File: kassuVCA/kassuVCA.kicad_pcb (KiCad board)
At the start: 2 copper layers, 49 x 59 mm, 20 parts, among them J1 Conn_02x05_Odd_Even, Q1 2N3904, Q2 2N3904, Q3 2N3904, U1 TL072

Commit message: switch to mbt3904 double transistor 2n3904 dual package
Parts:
- removed Q3: 2N3904, Package_TO_SOT_THT:TO-92L_Inline_Wide
- Q2: value 2N3904 -> MBT3904DW1; footprint Package_TO_SOT_THT:TO-92L_Inline_Wide -> Package_TO_SOT_SMD:SOT-363_SC-70-6
- moved Q2 2.51 mm to (125.5, 103.0), turned to 0 degrees
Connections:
- R10 pad 2: Net-(Q3-Pad3) -> Net-(Q2-Pad3)
- R11 pad 2: Net-(Q2-Pad3) -> Net-(Q2-Pad6)
- R12 pad 2: Net-(Q3-Pad3) -> Net-(Q2-Pad3)
- R7 pad 2: Net-(Q2-Pad3) -> Net-(Q2-Pad6)
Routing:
- net Net-(Q3-Pad3): track 60.0 -> 0.00 mm
- net Net-(Q2-Pad6): track 0.00 -> 37.9 mm
- net GND: track 0.00 -> 18.5 mm, vias 0 -> 1
- net Net-(Q2-Pad3): track 36.0 -> 50.3 mm
- net Net-(Q1-Pad1): track 47.5 -> 51.8 mm
- net Net-(R14-Pad1): track 35.7 -> 39.5 mm

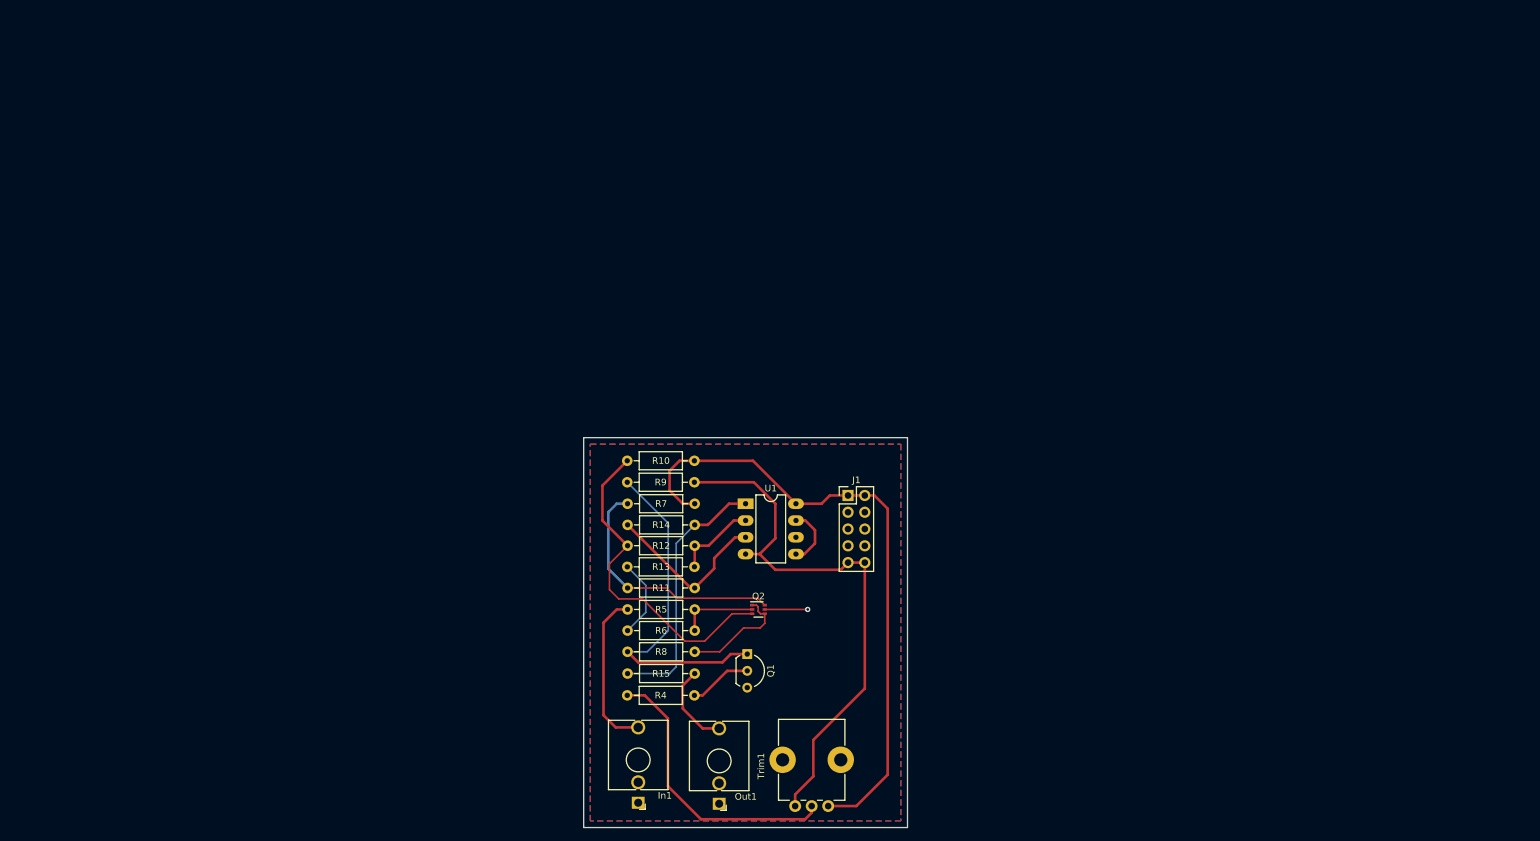
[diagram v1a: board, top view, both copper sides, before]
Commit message: VCA state working with jelly bean 2n3904 transistors
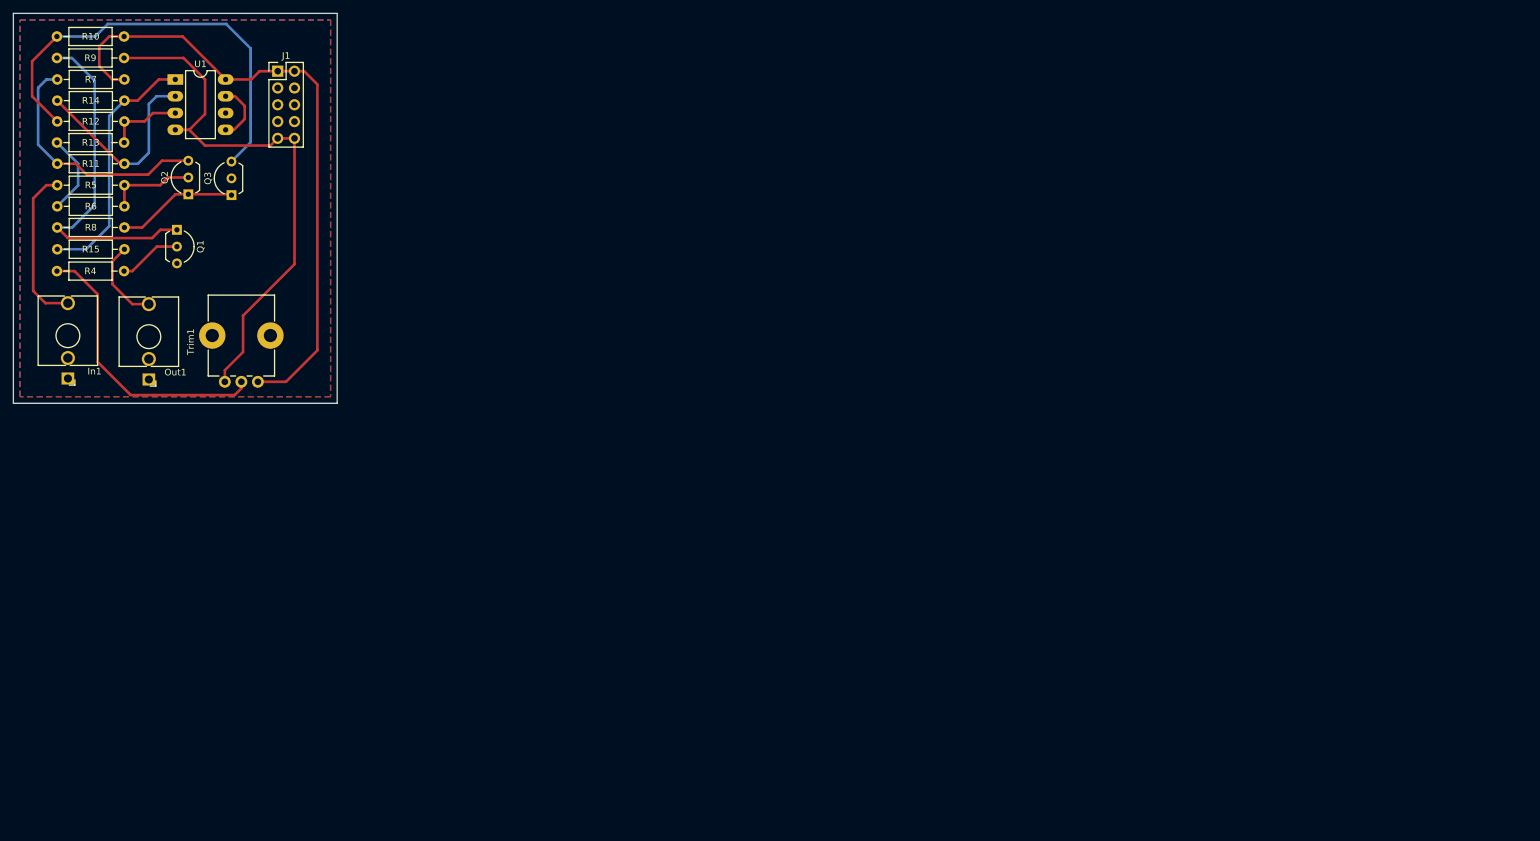
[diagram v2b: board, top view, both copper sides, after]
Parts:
- added Q3: 2N3904, Package_TO_SOT_THT:TO-92L_Inline_Wide, F.Cu at (45.7, 40.3)
- Q2: value MBT3904DW1 -> 2N3904; footprint Package_TO_SOT_SMD:SOT-363_SC-70-6 -> Package_TO_SOT_THT:TO-92L_Inline_Wide
- moved In1 107.6 mm to (20.9, 68.0)
- moved J1 107.6 mm to (52.7, 21.6)
- moved Out1 107.6 mm to (33.2, 68.2)
- moved Q1 107.6 mm to (37.5, 45.5)
- moved R10 107.6 mm to (29.4, 16.3)
- moved R11 107.6 mm to (29.5, 35.5)
- moved R12 107.6 mm to (29.5, 29.1)
- moved R13 107.6 mm to (19.3, 32.4)
- moved R14 107.6 mm to (29.5, 26.0)
- moved R15 107.6 mm to (19.3, 48.5)
- moved R4 107.6 mm to (29.4, 51.8)
- moved R5 107.6 mm to (29.5, 38.8)
- moved R6 107.6 mm to (19.3, 42.0)
- moved R7 107.6 mm to (29.5, 22.8)
- moved R8 107.6 mm to (29.5, 45.2)
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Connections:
- R10 pad 2: Net-(Q2-Pad3) -> Net-(Q3-Pad3)
- R11 pad 2: Net-(Q2-Pad6) -> Net-(Q2-Pad3)
- R12 pad 2: Net-(Q2-Pad3) -> Net-(Q3-Pad3)
- R7 pad 2: Net-(Q2-Pad6) -> Net-(Q2-Pad3)
- U1 pad 2: Net-(R12-Pad1) -> Net-(R11-Pad1)
- U1 pad 3: Net-(R11-Pad1) -> Net-(R12-Pad1)
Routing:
- net Net-(Q3-Pad3): track 0.00 -> 65.9 mm
- net Net-(Q2-Pad6): track 37.9 -> 0.00 mm
- net Net-(Q2-Pad3): track 50.3 -> 37.5 mm
- net GND: track 18.5 -> 12.3 mm, vias 1 -> 0
- net Net-(R11-Pad1): track 25.9 -> 30.4 mm
- net Net-(Q2-Pad1): track 16.7 -> 18.3 mm
- net Net-(Q2-Pad2): track 11.9 -> 13.4 mm
- net Net-(R14-Pad1): track 39.5 -> 38.3 mm
- net Net-(R12-Pad1): track 12.5 -> 11.4 mm
- added copper zone on B.Cu, net GND
- removed copper zone on B.Cu, net (none)
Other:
- net class Default: trace_width 0.25 -> 0.4

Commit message: mini transistor success!
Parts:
- removed Q3: 2N3904, Package_TO_SOT_THT:TO-92L_Inline_Wide
- Q2: value 2N3904 -> MBT3904DW1; footprint Package_TO_SOT_THT:TO-92L_Inline_Wide -> Package_TO_SOT_SMD:SOT-363_SC-70-6
- moved Q2 1.08 mm to (39.2, 39.1), turned to 0 degrees
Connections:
- R10 pad 2: Net-(Q3-Pad3) -> Net-(Q2-Pad3)
- R11 pad 2: Net-(Q2-Pad3) -> Net-(Q2-Pad6)
- R12 pad 2: Net-(Q3-Pad3) -> Net-(Q2-Pad3)
- R7 pad 2: Net-(Q2-Pad3) -> Net-(Q2-Pad6)
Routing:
- net Net-(Q3-Pad3): track 65.9 -> 0.00 mm
- net Net-(Q2-Pad6): track 0.00 -> 45.3 mm
- net GND: track 12.3 -> 29.0 mm
- net Net-(Q2-Pad3): track 37.5 -> 46.3 mm
- net Net-(Q2-Pad1): track 18.3 -> 16.2 mm
- net Net-(Q2-Pad2): track 13.4 -> 12.1 mm
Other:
- net class Default: trace_width 0.4 -> 0.25

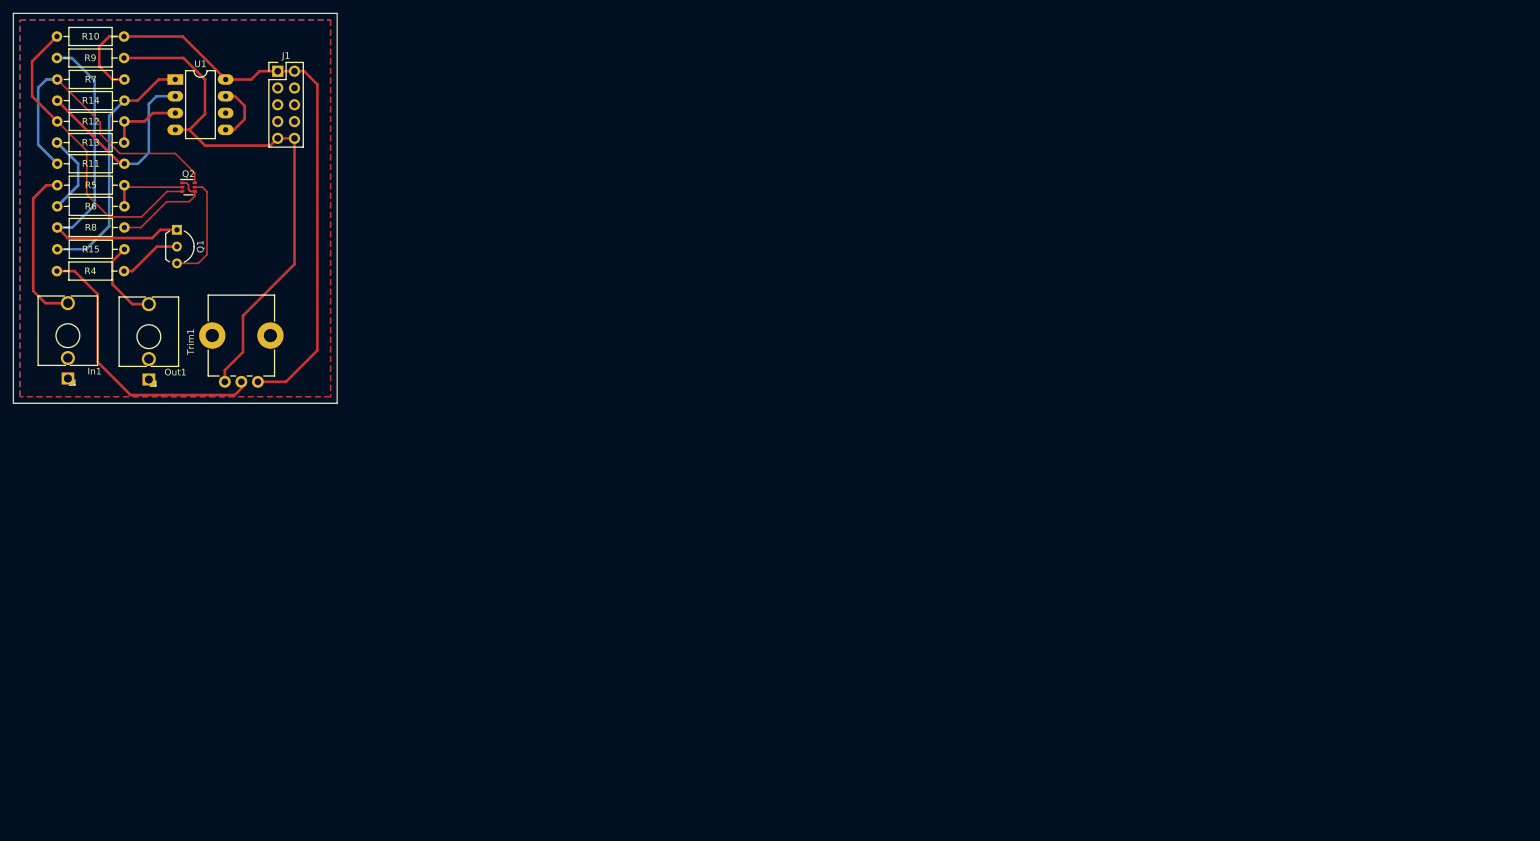
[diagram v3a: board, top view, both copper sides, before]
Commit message: WIP working towards a mixer
2 channels laid out with 207 resistors and TL074s. I need to move to TL072s and monolithic transistors in a few places for saner routing
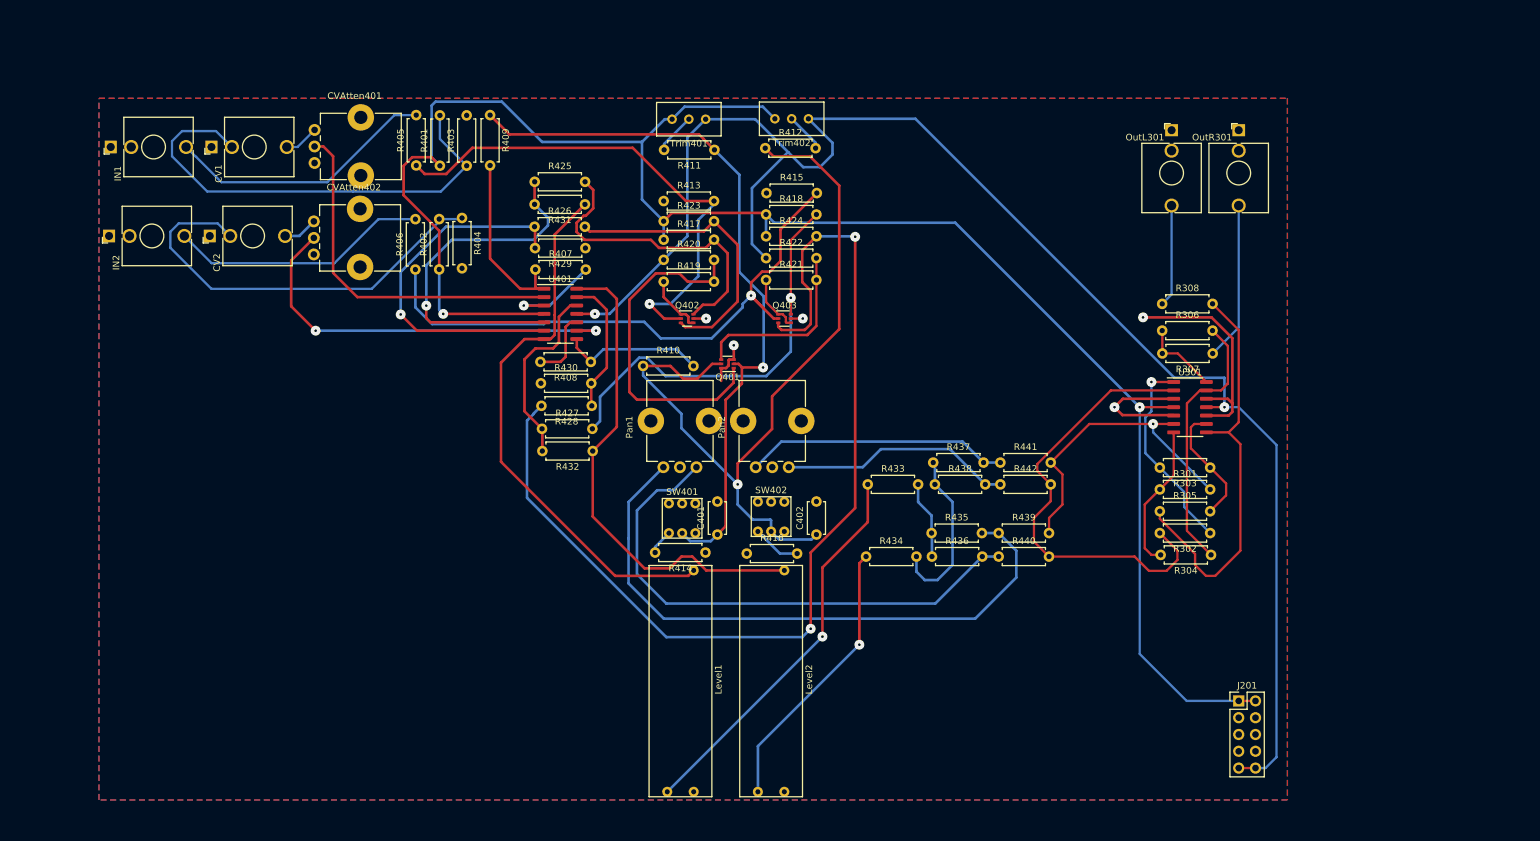
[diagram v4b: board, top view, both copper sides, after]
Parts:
- removed In1, Out1: AudioJack2_SwitchT, Connector_Audio:Jack_3.5mm_QingPu_WQP-PJ398SM_Vertical_CircularHoles
- removed J1: Conn_02x05_Odd_Even, Connector_PinHeader_2.54mm:PinHeader_2x05_P2.54mm_Vertical
- removed Q1: 2N3904, Package_TO_SOT_THT:TO-92L_Inline_Wide
- removed Q2: MBT3904DW1, Package_TO_SOT_SMD:SOT-363_SC-70-6
- removed R10, R11, R12, R7, R9: 10K, Resistor_THT:R_Axial_DIN0207_L6.3mm_D2.5mm_P10.16mm_Horizontal
- removed R13, R14, R5: 220K, Resistor_THT:R_Axial_DIN0207_L6.3mm_D2.5mm_P10.16mm_Horizontal
- removed R15, R6: 1K, Resistor_THT:R_Axial_DIN0207_L6.3mm_D2.5mm_P10.16mm_Horizontal
- removed R4, R8: 22K, Resistor_THT:R_Axial_DIN0207_L6.3mm_D2.5mm_P10.16mm_Horizontal
- removed Trim1: 100K, Potentiometer_THT:Potentiometer_Alps_RK09K_Single_Vertical
- removed U1: TL072, Package_DIP:DIP-8_W7.62mm_LongPads
- added C401: C, Capacitor_THT:C_Disc_D4.7mm_W2.5mm_P5.00mm, F.Cu at (119.2, 91.7)
- added C402: C, Capacitor_THT:C_Disc_D4.7mm_W2.5mm_P5.00mm, F.Cu at (134.2, 91.7)
- added CV1: AudioJack2_SwitchT, Connector_Audio:Jack_3.5mm_QingPu_WQP-PJ398SM_Vertical_CircularHoles, F.Cu at (42.7, 33.0)
- added CV2: AudioJack2_SwitchT, Connector_Audio:Jack_3.5mm_QingPu_WQP-PJ398SM_Vertical_CircularHoles, F.Cu at (42.4, 46.5)
- added CVAtten401: 100K, Potentiometer_THT:Potentiometer_Alps_RK09K_Single_Vertical, F.Cu at (58.3, 35.4)
- added CVAtten402: 100K, Potentiometer_THT:Potentiometer_Alps_RK09K_Single_Vertical, F.Cu at (58.2, 49.3)
- added IN1: AudioJack2_SwitchT, Connector_Audio:Jack_3.5mm_QingPu_WQP-PJ398SM_Vertical_CircularHoles, F.Cu at (27.4, 33.0)
- added IN2: AudioJack2_SwitchT, Connector_Audio:Jack_3.5mm_QingPu_WQP-PJ398SM_Vertical_CircularHoles, F.Cu at (27.2, 46.5)
- added J201: Conn_02x05_Odd_Even, Connector_PinHeader_2.54mm:PinHeader_2x05_P2.54mm_Vertical, F.Cu at (198.1, 116.8)
- added Level1: 100K, MixerFootprints:A-1623_SlidePot, F.Cu at (113.6, 113.8)
- added Level2: 100K, MixerFootprints:A-1623_SlidePot, F.Cu at (127.4, 113.8)
- added OutL301: AudioJack2_SwitchT, Connector_Audio:Jack_3.5mm_QingPu_WQP-PJ398SM_Vertical_CircularHoles, F.Cu at (188.0, 30.5)
- added OutR301: AudioJack2_SwitchT, Connector_Audio:Jack_3.5mm_QingPu_WQP-PJ398SM_Vertical_CircularHoles, F.Cu at (198.1, 30.5)
- added Pan1: 100K, Potentiometer_THT:Potentiometer_Alps_RK09K_Single_Vertical, F.Cu at (116.1, 81.5)
- added Pan2: 100K, Potentiometer_THT:Potentiometer_Alps_RK09K_Single_Vertical, F.Cu at (130.0, 81.5)
- added Q401: MBT3904DW1, Package_TO_SOT_SMD:SOT-363_SC-70-6, F.Cu at (120.8, 65.8)
- added Q402: MBT3904DW1, Package_TO_SOT_SMD:SOT-363_SC-70-6, F.Cu at (114.7, 59.0)
- added Q403: MBT3904DW1, Package_TO_SOT_SMD:SOT-363_SC-70-6, F.Cu at (129.4, 59.0)
- added R301: 39K, Resistor_THT:R_Axial_DIN0207_L6.3mm_D2.5mm_P7.62mm_Horizontal, F.Cu at (186.2, 84.8)
- added R302: 39K, Resistor_THT:R_Axial_DIN0207_L6.3mm_D2.5mm_P7.62mm_Horizontal, F.Cu at (193.8, 91.4)
- added R303: 2K, Resistor_THT:R_Axial_DIN0207_L6.3mm_D2.5mm_P7.62mm_Horizontal, F.Cu at (193.8, 81.5)
- added R304: 2K, Resistor_THT:R_Axial_DIN0207_L6.3mm_D2.5mm_P7.62mm_Horizontal, F.Cu at (193.9, 94.7)
- added R305: 100K, Resistor_THT:R_Axial_DIN0207_L6.3mm_D2.5mm_P7.62mm_Horizontal, F.Cu at (186.2, 88.1)
- added R306: 100K, Resistor_THT:R_Axial_DIN0207_L6.3mm_D2.5mm_P7.62mm_Horizontal, F.Cu at (186.5, 60.8)
- added R307: 1K, Resistor_THT:R_Axial_DIN0207_L6.3mm_D2.5mm_P7.62mm_Horizontal, F.Cu at (194.2, 64.3)
- added R308: 1K, Resistor_THT:R_Axial_DIN0207_L6.3mm_D2.5mm_P7.62mm_Horizontal, F.Cu at (186.5, 56.8)
- added R401: 220K, Resistor_THT:R_Axial_DIN0207_L6.3mm_D2.5mm_P7.62mm_Horizontal, F.Cu at (77.2, 35.9)
- added R402: 220K, Resistor_THT:R_Axial_DIN0207_L6.3mm_D2.5mm_P7.62mm_Horizontal, F.Cu at (77.1, 51.5)
- added R403: 100K, Resistor_THT:R_Axial_DIN0207_L6.3mm_D2.5mm_P7.62mm_Horizontal, F.Cu at (81.3, 35.9)
- added R404: 100K, Resistor_THT:R_Axial_DIN0207_L6.3mm_D2.5mm_P7.62mm_Horizontal, F.Cu at (80.6, 43.8)
- added R405: 220K, Resistor_THT:R_Axial_DIN0207_L6.3mm_D2.5mm_P7.62mm_Horizontal, F.Cu at (73.7, 35.8)
- added R406: 220K, Resistor_THT:R_Axial_DIN0207_L6.3mm_D2.5mm_P7.62mm_Horizontal, F.Cu at (73.5, 51.6)
- added R407: 47K, Resistor_THT:R_Axial_DIN0207_L6.3mm_D2.5mm_P7.62mm_Horizontal, F.Cu at (91.7, 51.6)
- added R408: 47K, Resistor_THT:R_Axial_DIN0207_L6.3mm_D2.5mm_P7.62mm_Horizontal, F.Cu at (100.1, 65.5)
- added R409: 22K, Resistor_THT:R_Axial_DIN0207_L6.3mm_D2.5mm_P7.62mm_Horizontal, F.Cu at (84.8, 28.2)
- added R410: 22K, Resistor_THT:R_Axial_DIN0207_L6.3mm_D2.5mm_P7.62mm_Horizontal, F.Cu at (108.0, 66.2)
- added R411: 22K, Resistor_THT:R_Axial_DIN0207_L6.3mm_D2.5mm_P7.62mm_Horizontal, F.Cu at (118.8, 33.5)
- added R412: 22K, Resistor_THT:R_Axial_DIN0207_L6.3mm_D2.5mm_P7.62mm_Horizontal, F.Cu at (126.5, 33.2)
- added R413: 1K, Resistor_THT:R_Axial_DIN0207_L6.3mm_D2.5mm_P7.62mm_Horizontal, F.Cu at (111.1, 41.2)
- added R414: 1K, Resistor_THT:R_Axial_DIN0207_L6.3mm_D2.5mm_P7.62mm_Horizontal, F.Cu at (117.4, 94.4)
- added R415: 1K, Resistor_THT:R_Axial_DIN0207_L6.3mm_D2.5mm_P7.62mm_Horizontal, F.Cu at (126.7, 40.0)
- added R416: 1K, Resistor_THT:R_Axial_DIN0207_L6.3mm_D2.5mm_P7.62mm_Horizontal, F.Cu at (123.7, 94.5)
- added R417: 10K, Resistor_THT:R_Axial_DIN0207_L6.3mm_D2.5mm_P7.62mm_Horizontal, F.Cu at (111.1, 47.0)
- added R418: 10K, Resistor_THT:R_Axial_DIN0207_L6.3mm_D2.5mm_P7.62mm_Horizontal, F.Cu at (126.6, 43.2)
- added R419: 22K, Resistor_THT:R_Axial_DIN0207_L6.3mm_D2.5mm_P7.62mm_Horizontal, F.Cu at (111.1, 53.4)
- added R420: 10K, Resistor_THT:R_Axial_DIN0207_L6.3mm_D2.5mm_P7.62mm_Horizontal, F.Cu at (111.1, 50.1)
- added R421: 22K, Resistor_THT:R_Axial_DIN0207_L6.3mm_D2.5mm_P7.62mm_Horizontal, F.Cu at (126.6, 53.1)
- added R422: 10K, Resistor_THT:R_Axial_DIN0207_L6.3mm_D2.5mm_P7.62mm_Horizontal, F.Cu at (126.6, 49.8)
- added R423: 10K, Resistor_THT:R_Axial_DIN0207_L6.3mm_D2.5mm_P7.62mm_Horizontal, F.Cu at (111.1, 44.2)
- added R424: 10K, Resistor_THT:R_Axial_DIN0207_L6.3mm_D2.5mm_P7.62mm_Horizontal, F.Cu at (126.6, 46.5)
- added R425: 10K, Resistor_THT:R_Axial_DIN0207_L6.3mm_D2.5mm_P7.62mm_Horizontal, F.Cu at (91.6, 38.3)
- added R426: 10K, Resistor_THT:R_Axial_DIN0207_L6.3mm_D2.5mm_P7.62mm_Horizontal, F.Cu at (91.6, 45.1)
- added R427: 10K, Resistor_THT:R_Axial_DIN0207_L6.3mm_D2.5mm_P7.62mm_Horizontal, F.Cu at (92.7, 75.7)
- added R428: 10K, Resistor_THT:R_Axial_DIN0207_L6.3mm_D2.5mm_P7.62mm_Horizontal, F.Cu at (100.2, 72.2)
- added R429: 220K, Resistor_THT:R_Axial_DIN0207_L6.3mm_D2.5mm_P7.62mm_Horizontal, F.Cu at (99.3, 48.3)
- added R430: 220K, Resistor_THT:R_Axial_DIN0207_L6.3mm_D2.5mm_P7.62mm_Horizontal, F.Cu at (92.5, 68.8)
- added R431: 220K, Resistor_THT:R_Axial_DIN0207_L6.3mm_D2.5mm_P7.62mm_Horizontal, F.Cu at (99.2, 41.7)
- added R432: 220K, Resistor_THT:R_Axial_DIN0207_L6.3mm_D2.5mm_P7.62mm_Horizontal, F.Cu at (100.4, 79.0)
- added R433: 220K, Resistor_THT:R_Axial_DIN0207_L6.3mm_D2.5mm_P7.62mm_Horizontal, F.Cu at (142.0, 84.1)
- added R434: 220K, Resistor_THT:R_Axial_DIN0207_L6.3mm_D2.5mm_P7.62mm_Horizontal, F.Cu at (141.7, 95.0)
- added R435: 22K, Resistor_THT:R_Axial_DIN0207_L6.3mm_D2.5mm_P7.62mm_Horizontal, F.Cu at (151.6, 91.4)
- added R436: 22K, Resistor_THT:R_Axial_DIN0207_L6.3mm_D2.5mm_P7.62mm_Horizontal, F.Cu at (151.7, 95.0)
- added R437: 22K, Resistor_THT:R_Axial_DIN0207_L6.3mm_D2.5mm_P7.62mm_Horizontal, F.Cu at (151.9, 80.8)
- added R438: 22K, Resistor_THT:R_Axial_DIN0207_L6.3mm_D2.5mm_P7.62mm_Horizontal, F.Cu at (152.1, 84.1)
- added R439: 22K, Resistor_THT:R_Axial_DIN0207_L6.3mm_D2.5mm_P7.62mm_Horizontal, F.Cu at (161.8, 91.4)
- added R440: 22K, Resistor_THT:R_Axial_DIN0207_L6.3mm_D2.5mm_P7.62mm_Horizontal, F.Cu at (161.8, 95.0)
- added R441: 22K, Resistor_THT:R_Axial_DIN0207_L6.3mm_D2.5mm_P7.62mm_Horizontal, F.Cu at (162.1, 80.8)
- added R442: 22K, Resistor_THT:R_Axial_DIN0207_L6.3mm_D2.5mm_P7.62mm_Horizontal, F.Cu at (162.1, 84.1)
- added SW401: SW_DPDT_x2, MixerFootprints:A-330-6mm-dpdt, F.Cu at (113.9, 89.2)
- added SW402: SW_DPDT_x2, MixerFootprints:A-330-6mm-dpdt, F.Cu at (127.4, 89.0)
- added Trim401: 100K, Potentiometer_THT:Potentiometer_Bourns_3296W_Vertical, F.Cu at (112.4, 28.8)
- added Trim402: 100K, Potentiometer_THT:Potentiometer_Bourns_3296W_Vertical, F.Cu at (127.9, 28.8)
- added U301: TL074, Package_SO:SOIC-14_3.9x8.7mm_P1.27mm, F.Cu at (190.8, 72.4)
- added U401: TL074, Package_SO:SOIC-14_3.9x8.7mm_P1.27mm, F.Cu at (95.5, 58.3)
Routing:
- net +12V: track 96.5 -> 281.1 mm, vias 0 -> 2
- net -12V: track 82.9 -> 239.8 mm, vias 0 -> 2
- net Net-(Q403-Pad3): track 0.00 -> 155.8 mm, vias 0 -> 2
- net Net-(C402-Pad1): track 0.00 -> 121.0 mm, vias 0 -> 1
- net Net-(C401-Pad1): track 0.00 -> 109.8 mm, vias 0 -> 1
- net Net-(Pan1-Pad3): track 0.00 -> 93.6 mm
- net Net-(Q403-Pad2): track 0.00 -> 90.3 mm, vias 0 -> 1
- net Net-(Level1-Pad3): track 0.00 -> 83.2 mm
- net Net-(Pan1-Pad1): track 0.00 -> 80.9 mm
- net Net-(Q402-Pad2): track 0.00 -> 77.7 mm, vias 0 -> 1
- net Net-(Level2-Pad3): track 0.00 -> 75.0 mm
- net Net-(CV1-PadTN): track 0.00 -> 70.7 mm
- net Level1L: track 0.00 -> 68.3 mm
- net Net-(Q403-Pad6): track 0.00 -> 64.2 mm, vias 0 -> 1
- net Net-(CV2-PadTN): track 0.00 -> 64.2 mm
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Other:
- board outline removed
- net class Default: clearance 0.3 -> 0.25; trace_width 0.25 -> 0.35
- rule trace_clearance: 0.3 -> 0.25
